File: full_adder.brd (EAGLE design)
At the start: 100 x 120 mm, 91 parts, among them T101 TPH1R712MD, T102 TPH1R712MD, U1001 FDS6892A, U1002 FDS6892A, U1003 FDS6892A, U101 ATTINY45-20P, U201 CD4052BE, U202 CD4052BE, U203 CD4052BE, U401 KM28C65A-20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

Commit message: basic layout complete
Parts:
- moved T102 212.5 mm to (93.7, 9.70), turned to 90 degrees
- moved C201 210.5 mm to (88.2, 47.2)
- moved T101 203.6 mm to (93.7, 17.3), turned to 90 degrees
- moved U1003 173.0 mm to (69.8, 56.0)
- moved U1002 160.6 mm to (69.9, 66.0)
- moved C501 158.5 mm to (56.3, 18.6)
- moved C101 157.6 mm to (33.7, 18.6)
- moved C601 152.2 mm to (37.9, 85.7), turned to 90 degrees
- moved C602 151.0 mm to (44.3, 82.1)
- moved U1001 148.7 mm to (70.1, 75.0)
- moved C305 145.8 mm to (67.5, 37.6)
- moved C603 145.2 mm to (57.6, 82.6)
- moved C202 136.5 mm to (78.2, 4.60)
- moved U101 134.7 mm to (80.8, 12.9), turned to 90 degrees
- moved C701 133.0 mm to (22.0, 36.6)
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
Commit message: Components placed
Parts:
- U101: value ATTINY45-20P -> ATTINY85
- moved LED101 217.0 mm to (87.2, 6.00)
- moved TP102 210.1 mm to (81.0, 23.0)
- moved R101 209.7 mm to (80.0, 6.00), turned to 180 degrees
- moved TP103 208.6 mm to (73.0, 23.0)
- moved TP101 208.0 mm to (85.0, 23.0)
- moved R102 204.7 mm to (72.0, 14.0), turned to 270 degrees
- moved R404 134.4 mm to (76.0, 33.0), turned to 180 degrees
- moved TP104 130.7 mm to (77.0, 23.0)
- moved R403 127.5 mm to (76.0, 36.0)
- moved R402 120.5 mm to (76.0, 39.0)
- moved R401 113.6 mm to (76.0, 42.0)
- moved C202 106.4 mm to (43.0, 105.0)
- moved C203 104.3 mm to (67.0, 105.0)
- moved R1005 102.1 mm to (37.0, 39.0), turned to 90 degrees
- moved R1004 101.2 mm to (43.5, 39.0), turned to 90 degrees
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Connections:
- new net N$45: R401.2, U401.11
- new net N$46: R402.2, U401.12
- new net N$47: R403.2, U401.13
- new net N$48: R407.1, U401.18
- new net N$49: R406.1, U401.17
- new net N$50: R405.1, U401.16
- new net N$51: R404.1, U401.15
- net BCD_DATA_A: no longer R401.2, U401.11
- net BCD_DATA_B: no longer R402.2, U401.12
- net BCD_DATA_C: no longer R403.2, U401.13
- net BCD_DATA_D: no longer R404.1, U401.15
- net BCD_DATA_E: no longer R405.1, U401.16
- net BCD_DATA_F: no longer R406.1, U401.17
- net BCD_DATA_G: no longer R407.1, U401.18
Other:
- board text added: "BAT_LED"
- board text added: "LSB"
- board text added: "MSB"

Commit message: routing v1 done
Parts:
- moved C1 188.1 mm to (91.1, 26.6), flipped to the bottom
- moved R603 120.7 mm to (21.1, 73.1), flipped to the bottom
- moved S904 113.7 mm to (7.00, 75.0), flipped to the bottom, turned to 270 degrees
- moved S903 97.5 mm to (7.00, 83.0), flipped to the bottom, turned to 270 degrees
- moved S908 93.8 mm to (7.00, 43.0), flipped to the bottom, turned to 270 degrees
- moved S902 81.0 mm to (7.00, 67.0), flipped to the bottom, turned to 270 degrees
- moved S907 75.5 mm to (7.00, 51.0), flipped to the bottom, turned to 270 degrees
- moved S901 68.5 mm to (7.00, 99.0), flipped to the bottom, turned to 270 degrees
- moved S906 57.2 mm to (7.00, 59.0), flipped to the bottom, turned to 270 degrees
- moved R404 39.1 mm to (85.0, 71.0), turned to 90 degrees
- moved S905 34.0 mm to (7.00, 91.0), flipped to the bottom, turned to 270 degrees
- moved C201 14.0 mm to (33.0, 105.0), turned to 180 degrees
- moved C202 14.0 mm to (57.0, 105.0), turned to 180 degrees
- moved C203 14.0 mm to (81.0, 105.0), turned to 180 degrees
- moved R405 6.00 mm to (88.0, 71.0)
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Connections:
- new net N$52: U701.2, U701.6
- net C1: no longer U701.2, U701.6
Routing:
- net A3: track 0.00 -> 196.2 mm, vias 0 -> 4
- net B3: track 0.00 -> 181.6 mm, vias 0 -> 2
- net S0: track 0.00 -> 171.3 mm, vias 0 -> 6
- net A2: track 0.00 -> 168.2 mm, vias 0 -> 3
- net BCD_DATA_G: track 0.00 -> 167.3 mm, vias 0 -> 8
- net B2: track 0.00 -> 164.7 mm, vias 0 -> 3
- net BCD_DATA_F: track 0.00 -> 162.5 mm, vias 0 -> 5
- net S1: track 0.00 -> 161.5 mm, vias 0 -> 5
- net A1: track 0.00 -> 155.6 mm, vias 0 -> 3
- net BCD_DATA_A: track 0.00 -> 152.7 mm, vias 0 -> 5
- net BCD_DATA_E: track 0.00 -> 149.3 mm, vias 0 -> 8
- net BCD_DATA_B: track 0.00 -> 144.4 mm, vias 0 -> 3
- net C2: track 0.00 -> 143.9 mm
- net C1: track 0.00 -> 143.4 mm, vias 0 -> 1
- net S2: track 0.00 -> 142.5 mm, vias 0 -> 3
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- added copper zone on layer 1, net N$41
- added copper zone on layer 1, net N$42
- added copper zone on layer 1, net VCC

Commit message: drc errors, power planes
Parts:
- removed LED1101, LED1102, LED1103, LED1104, LED1105, LED1106, LED1107, LED1108: (no value), led:LED3MM
- removed R1101, R1102, R1103, R1104, R1105, R1106, R1107, R1108: 2k2, rcl:R1206
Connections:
- removed net N$18: LED1101.A, R1101.1
- removed net N$19: LED1102.A, R1102.1
- removed net N$20: LED1103.A, R1103.1
- removed net N$21: LED1104.A, R1104.1
- removed net N$22: LED1105.A, R1105.1
- removed net N$23: LED1106.A, R1106.1
- removed net N$24: LED1107.A, R1107.1
- removed net N$25: LED1108.A, R1108.1
- net A0: no longer R1101.2
- net A1: no longer R1102.2
- net A2: no longer R1103.2
- net A3: no longer R1104.2
- net B0: no longer R1105.2
- net B1: no longer R1106.2
- net B2: no longer R1107.2
- net B3: no longer R1108.2
- net GND: no longer LED1101.K, LED1102.K, LED1103.K, LED1104.K, LED1105.K, LED1106.K, LED1107.K, LED1108.K
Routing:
- net VCC: track 71.9 -> 107.4 mm, vias 0 -> 6
- net GND: track 0.00 -> 21.8 mm, vias 0 -> 1
- net N$43: track 21.6 -> 24.8 mm
- net N$30: track 11.2 -> 14.3 mm
- net N$15: track 20.7 -> 17.9 mm
- net BCD_DATA_C: track 140.3 -> 142.9 mm
- net A0: track 137.9 -> 140.1 mm
- net B0: track 140.2 -> 142.1 mm
- net A3: track 196.2 -> 197.9 mm
- net COUT_3: track 104.7 -> 105.6 mm
- net S0: track 171.3 -> 171.8 mm
- net BCD_DATA_E: track 149.3 -> 149.2 mm, vias 8 -> 7
- net BCD_DATA_D: vias 7 -> 5
- added copper zone on layer 1, net GND
- added copper zone on layer 16, net N$41
- added copper zone on layer 16, net VCC

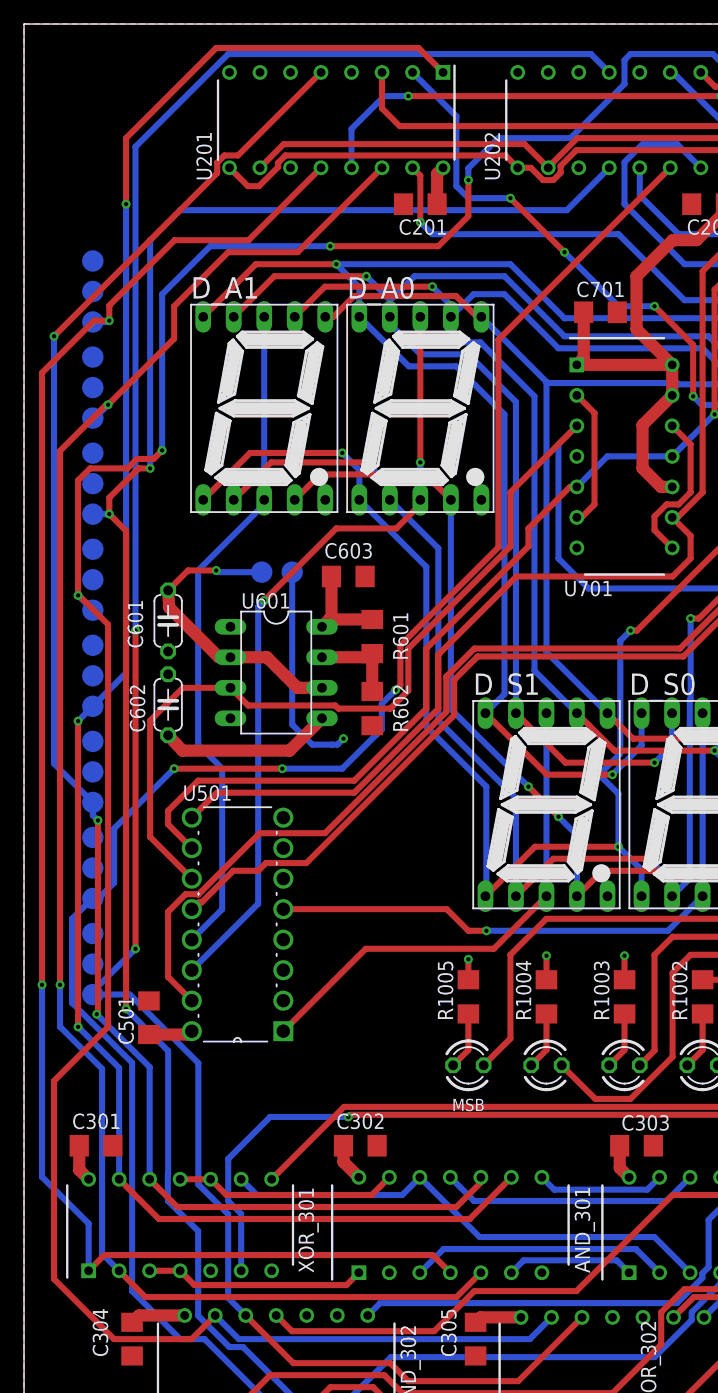
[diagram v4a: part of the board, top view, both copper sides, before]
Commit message: fixing airwires
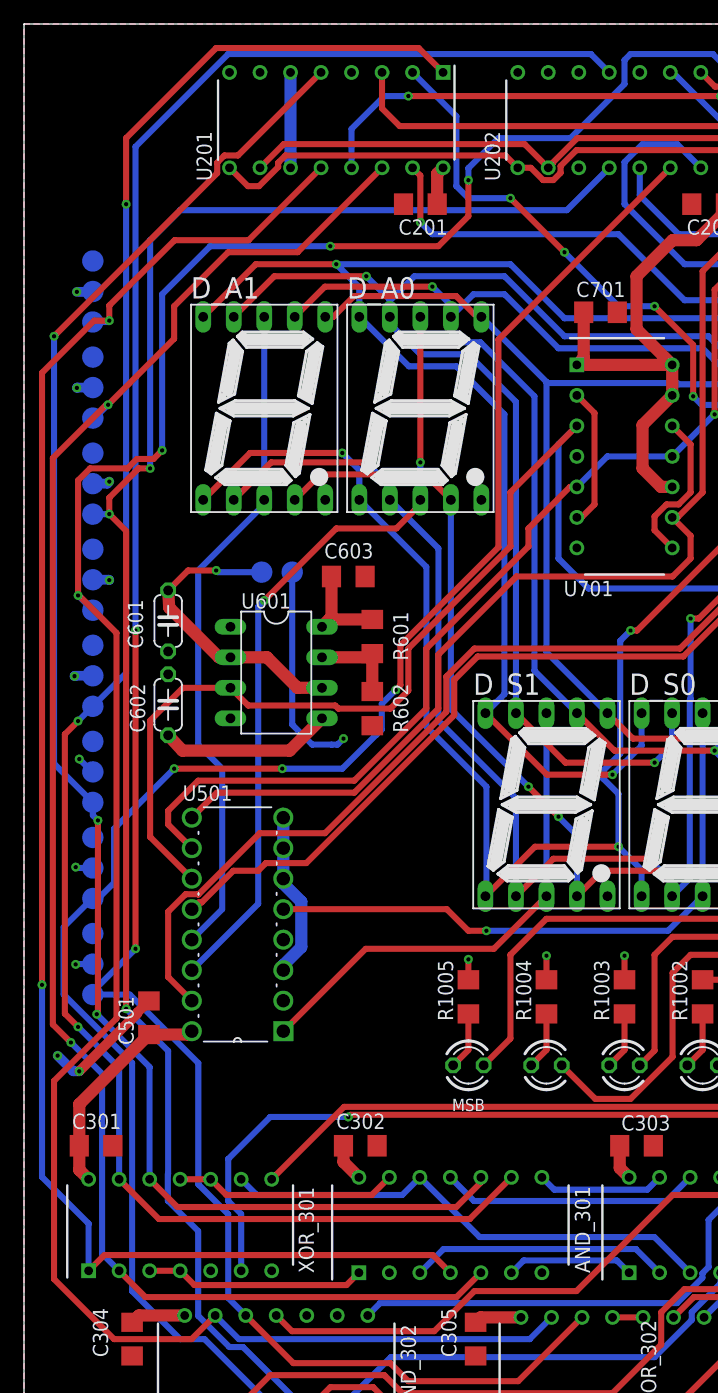
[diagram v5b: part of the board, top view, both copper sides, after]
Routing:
- net GND: track 21.8 -> 65.9 mm, vias 1 -> 11
- net VCC: track 107.4 -> 119.0 mm
- net N$10: track 0.00 -> 2.54 mm
- net A1: track 155.6 -> 156.5 mm
- net A3: track 197.9 -> 198.5 mm
- net B2: track 164.7 -> 165.3 mm

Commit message: DRC passed
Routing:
- net GND: track 65.9 -> 296.2 mm, vias 11 -> 31
- net VCC: track 119.0 -> 195.2 mm, vias 6 -> 14
- net COUT_2: track 10.5 -> 40.1 mm, vias 0 -> 2
- net N$10: track 2.54 -> 29.7 mm, vias 0 -> 1
- net A1: track 156.5 -> 160.1 mm
- net N$15: track 17.9 -> 20.7 mm
- net N$41: track 4.48 -> 7.18 mm
- net A3: track 198.5 -> 199.5 mm
- net B1: track 135.2 -> 136.1 mm
- net A0: track 140.1 -> 141.0 mm
- net N$12: track 47.9 -> 47.1 mm
- net N$13: track 39.2 -> 39.9 mm
- net A2: track 168.4 -> 169.1 mm

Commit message: gate resistor
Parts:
- R1001, R1002, R1003, R1004, R1005: value 2k2 -> 10k
- R102: value 100k -> 10k
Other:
- board text added: "Jakob Soukup 2020"
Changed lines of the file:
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@@
 <setting verticaltext="up"/>
 </settings>
-<grid distance="0.1" unitdist="mm" unit="mm" style="lines" multiple="1" display="yes" altdistance="5" altunitdist="mil" altunit="mm"/>
+<grid distance="1" unitdist="mm" unit="mm" style="lines" multiple="1" display="yes" altdistance="5" altunitdist="mil" altunit="mm"/>
 <layers>
 <layer number="1" name="Top" color="4" fill="1" visible="yes" active="yes"/>
@@
 <layer number="20" name="Dimension" color="24" fill="1" visible="yes" active="yes"/>
 <layer number="21" name="tPlace" color="7" fill="1" visible="yes" active="yes"/>
-<layer number="22" name="bPlace" color="7" fill="1" visible="no" active="yes"/>
+<layer number="22" name="bPlace" color="7" fill="1" visible="yes" active="yes"/>
 <layer number="23" name="tOrigins" color="15" fill="1" visible="yes" active="yes"/>
 <layer number="24" name="bOrigins" color="15" fill="1" visible="no" active="yes"/>
 <layer number="25" name="tNames" color="7" fill="1" visible="yes" active="yes"/>
-<layer number="26" name="bNames" color="7" fill="1" visible="no" active="yes"/>
-<layer number="27" name="tValues" color="7" fill="1" visible="no" active="yes"/>
-<layer number="28" name="bValues" color="7" fill="1" visible="no" active="yes"/>
+<layer number="26" name="bNames" color="7" fill="1" visible="yes" active="yes"/>
+<layer number="27" name="tValues" color="7" fill="1" visible="yes" active="yes"/>
+<layer number="28" name="bValues" color="7" fill="1" visible="yes" active="yes"/>
 <layer number="29" name="tStop" color="7" fill="3" visible="no" active="yes"/>
 <layer number="30" name="bStop" color="7" fill="6" visible="no" active="yes"/>
@@
 <layer number="43" name="vRestrict" color="2" fill="10" visible="no" active="yes"/>
 <layer number="44" name="Drills" color="7" fill="1" visible="no" active="yes"/>
-<layer number="45" name="Holes" color="7" fill="1" visible="no" active="yes"/>
+<layer number="45" name="Holes" color="7" fill="1" visible="yes" active="yes"/>
 <layer number="46" name="Milling" color="3" fill="1" visible="no" active="yes"/>
 <layer number="47" name="Measures" color="7" fill="1" visible="no" active="yes"/>
@@
 <text x="37" y="30" size="1.016" layer="25" align="center">MSB</text>
 <text x="84" y="2" size="1.016" layer="25">BAT_LED</text>
+<text x="97.5" y="1.2" size="1.778" layer="26" rot="MR0">Jakob Soukup 2020</text>
+<hole x="5" y="115" drill="3.3"/>
+<hole x="95" y="115" drill="3.3"/>
+<hole x="95" y="5" drill="3.3"/>
+<hole x="5" y="5" drill="3.3"/>
 </plain>
 <attributes>
@@
 <attribute name="RS_PART_NUMBER" value="0307519P" x="80.69" y="38.98" size="1.778" layer="27" rot="R90" display="off"/>
 <attribute name="RS_PRICE-STOCK" value="http://uk.rs-online.com/web/p/products/0307519P" x="80.69" y="38.98" size="1.778" layer="27" rot="R90" display="off"/>
-<attribute name="VALUE" x="19" y="8.5" size="1.27" layer="27" rot="R90" align="center"/>
+<attribute name="VALUE" x="21.5" y="9" size="1.27" layer="27" rot="R180" align="center"/>
 </element>
 <element name="C1" library="custom" package="BATTERY_CONNECTOR" value="BATTERY_CONNECTOR" x="91.13" y="26.59" smashed="yes" rot="MR0">
@@
 <attribute name="VALUE" x="56" y="20" size="1.27" layer="27" rot="R90" align="center"/>
 </element>
-<element name="R1001" library="rcl" library_urn="urn:adsk.eagle:library:334" package="R1206" package3d_urn="urn:adsk.eagle:package:23540/2" value="2k2" x="63" y="39" smashed="yes" rot="R90">
+<element name="R1001" library="rcl" library_urn="urn:adsk.eagle:library:334" package="R1206" package3d_urn="urn:adsk.eagle:package:23540/2" value="10k" x="63" y="39" smashed="yes" rot="R90">
 <attribute name="NAME" x="61.73" y="37" size="1.27" layer="25" rot="R90"/>
 <attribute name="POPULARITY" value="41" x="158.25" y="56.78" size="1.778" layer="27" rot="R90" display="off"/>
 <attribute name="SPICEPREFIX" value="R" x="158.25" y="56.78" size="1.778" layer="27" rot="R90" display="off"/>
 </element>
-<element name="R1002" library="rcl" library_urn="urn:adsk.eagle:library:334" package="R1206" package3d_urn="urn:adsk.eagle:package:23540/2" value="2k2" x="56.5" y="39" smashed="yes" rot="R90">
+<element name="R1002" library="rcl" library_urn="urn:adsk.eagle:library:334" package="R1206" package3d_urn="urn:adsk.eagle:package:23540/2" value="10k" x="56.5" y="39" smashed="yes" rot="R90">
 <attribute name="NAME" x="55.23" y="37" size="1.27" layer="25" rot="R90"/>
 <attribute name="POPULARITY" value="41" x="151.75" y="64.4" size="1.778" layer="27" rot="R90" display="off"/>
 <attribute name="SPICEPREFIX" value="R" x="151.75" y="64.4" size="1.778" layer="27" rot="R90" display="off"/>
 </element>
-<element name="R1003" library="rcl" library_urn="urn:adsk.eagle:library:334" package="R1206" package3d_urn="urn:adsk.eagle:package:23540/2" value="2k2" x="50" y="39" smashed="yes" rot="R90">
+<element name="R1003" library="rcl" library_urn="urn:adsk.eagle:library:334" package="R1206" package3d_urn="urn:adsk.eagle:package:23540/2" value="10k" x="50" y="39" smashed="yes" rot="R90">
 <attribute name="NAME" x="48.73" y="37" size="1.27" layer="25" rot="R90"/>
 <attribute name="POPULARITY" value="41" x="145.25" y="72.02" size="1.778" layer="27" rot="R90" display="off"/>
 <attribute name="SPICEPREFIX" value="R" x="145.25" y="72.02" size="1.778" layer="27" rot="R90" display="off"/>
 </element>
-<element name="R1004" library="rcl" library_urn="urn:adsk.eagle:library:334" package="R1206" package3d_urn="urn:adsk.eagle:package:23540/2" value="2k2" x="43.5" y="39" smashed="yes" rot="R90">
+<element name="R1004" library="rcl" library_urn="urn:adsk.eagle:library:334" package="R1206" package3d_urn="urn:adsk.eagle:package:23540/2" value="10k" x="43.5" y="39" smashed="yes" rot="R90">
 <attribute name="NAME" x="42.23" y="37" size="1.27" layer="25" rot="R90"/>
 <attribute name="POPULARITY" value="41" x="138.75" y="79.64" size="1.778" layer="27" rot="R90" display="off"/>
 <attribute name="SPICEPREFIX" value="R" x="138.75" y="79.64" size="1.778" layer="27" rot="R90" display="off"/>
 </element>
-<element name="R1005" library="rcl" library_urn="urn:adsk.eagle:library:334" package="R1206" package3d_urn="urn:adsk.eagle:package:23540/2" value="2k2" x="37" y="39" smashed="yes" rot="R90">
+<element name="R1005" library="rcl" library_urn="urn:adsk.eagle:library:334" package="R1206" package3d_urn="urn:adsk.eagle:package:23540/2" value="10k" x="37" y="39" smashed="yes" rot="R90">
 <attribute name="NAME" x="35.73" y="37" size="1.27" layer="25" rot="R90"/>
 <attribute name="POPULARITY" value="41" x="132.25" y="87.26" size="1.778" layer="27" rot="R90" display="off"/>
@@
 <attribute name="SPICEPREFIX" value="R" x="-26.68" y="107.6" size="1.778" layer="27" rot="R180" display="off"/>
 </element>
-<element name="R102" library="rcl" library_urn="urn:adsk.eagle:library:334" package="R1206" package3d_urn="urn:adsk.eagle:package:23540/2" value="100k" x="72" y="14.03" smashed="yes" rot="R270">
+<element name="R102" library="rcl" library_urn="urn:adsk.eagle:library:334" package="R1206" package3d_urn="urn:adsk.eagle:package:23540/2" value="10k" x="72" y="14.03" smashed="yes" rot="R270">
 <attribute name="NAME" x="73.27" y="15.3" size="1.27" layer="25" rot="R270"/>
 <attribute name="POPULARITY" value="41" x="-29.6" y="-99" size="1.778" layer="27" rot="R270" display="off"/>
@@
 <attribute name="MOUSER_PART_NUMBER" value="" x="107.42" y="105.02" size="1.778" layer="27" rot="R90" display="off"/>
 <attribute name="MOUSER_PRICE-STOCK" value="" x="107.42" y="105.02" size="1.778" layer="27" rot="R90" display="off"/>
-<attribute name="NAME" x="52" y="8.5" size="1.27" layer="25" rot="R90" align="center"/>
+<attribute name="NAME" x="60" y="8.5" size="1.27" layer="25" rot="R90" align="center"/>
 <attribute name="RS_PART_NUMBER" value="0644234" x="107.42" y="105.02" size="1.778" layer="27" rot="R90" display="off"/>
 <attribute name="RS_PRICE-STOCK" value="http://uk.rs-online.com/web/p/products/0644234" x="107.42" y="105.02" size="1.778" layer="27" rot="R90" display="off"/>
-<attribute name="VALUE" x="47" y="8.5" size="1.27" layer="27" rot="R90" align="center"/>
+<attribute name="VALUE" x="49.5" y="9" size="1.27" layer="27" rot="R180" align="center"/>
 </element>
 </elements>
@@
 <wire x1="93.55" y1="13.3" x2="95.455" y2="11.395" width="0.508" layer="1"/>
 <wire x1="95.455" y1="11.395" x2="95.95" y2="11.395" width="0.508" layer="1"/>
-<wire x1="5.7" y1="44.3" x2="5.73" y2="44.27" width="0.508" layer="16"/>
 <wire x1="5.73" y1="44.27" x2="5.73" y2="44.03" width="0.508" layer="16"/>
 <wire x1="5.73" y1="44.03" x2="4.7" y2="43" width="0.508" layer="16"/>
